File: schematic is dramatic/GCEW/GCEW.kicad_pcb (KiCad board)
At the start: 2 copper layers, 100 x 90 mm, 52 parts, among them J1 Conn_01x08, J2 Conn_01x02, J3 Conn_02x03_Odd_Even, J4 Conn_02x03_Odd_Even, J5 Conn_02x02_Odd_Even, M1 BLDC_Motor, U1 LM26CIM5-VHA, U2 DRV8323RH, U3 IPB029N06N, U4 IPB029N06N, U5 IPB029N06N, U6 IPB029N06N, U7 IPB029N06N, U8 IPB029N06N, U9 BLDC_Hall_Sensor

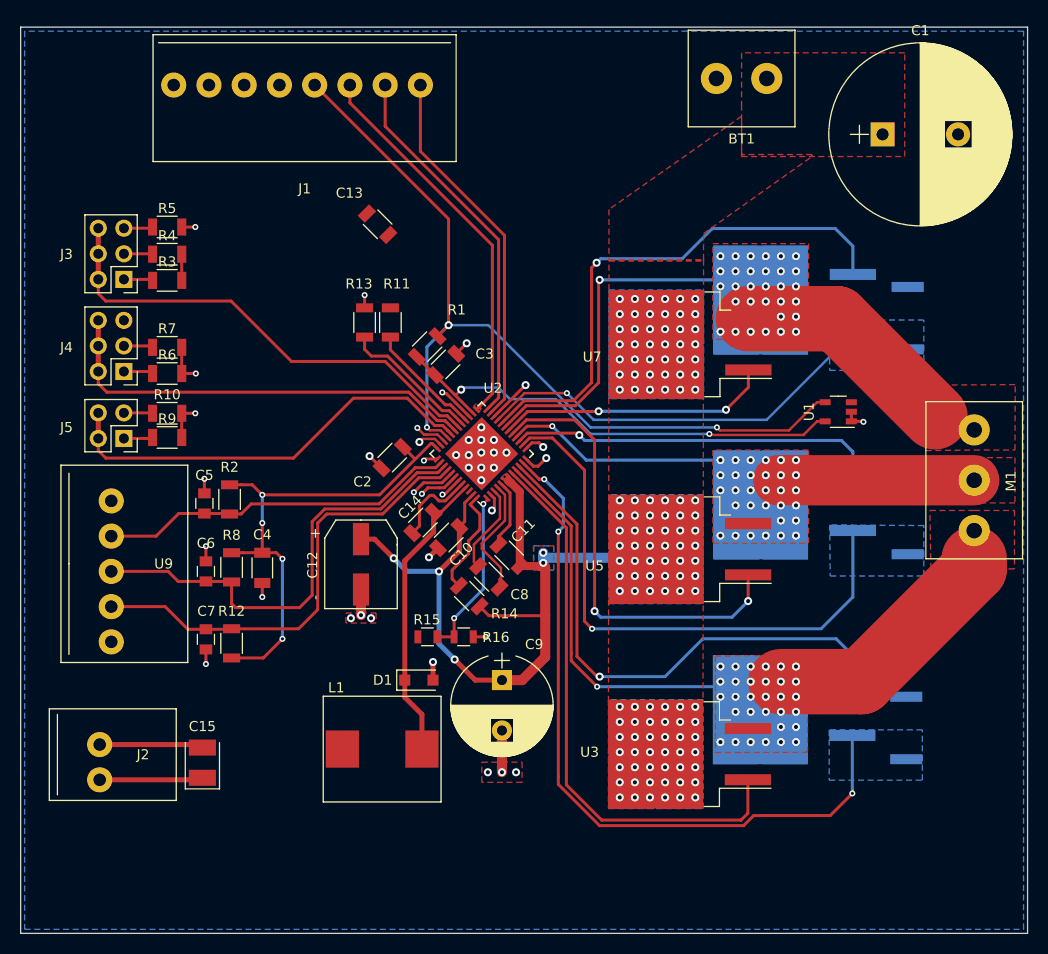
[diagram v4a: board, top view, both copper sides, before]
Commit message: GCEW Motor Controller PCB Update 1
Completed GCEW Motor Controller PCB Design.
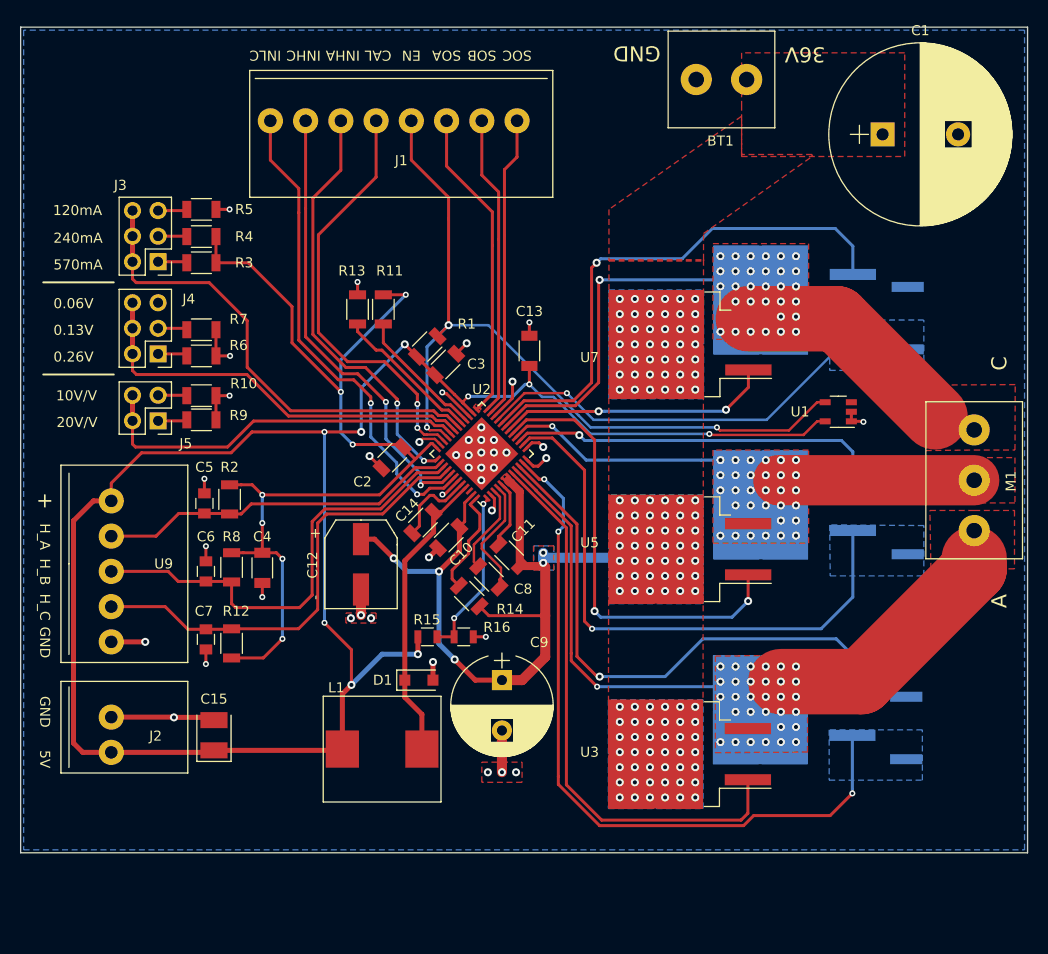
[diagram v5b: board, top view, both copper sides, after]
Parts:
- moved C13 19.6 mm to (165.5, 97.2), turned to 90 degrees
- moved J1 10.2 mm to (152.8, 75.6)
- moved J3 3.82 mm to (128.7, 88.3)
- moved J4 3.82 mm to (128.7, 97.5)
- moved J5 3.82 mm to (128.7, 104.1)
- moved R10 3.82 mm to (132.9, 101.6)
- moved R3 3.82 mm to (132.9, 88.4)
- moved R4 3.82 mm to (132.9, 85.8)
- moved R5 3.82 mm to (132.9, 83.1)
- moved R6 3.82 mm to (132.9, 97.7)
- moved R7 3.82 mm to (132.9, 95.0)
- moved R9 3.82 mm to (132.9, 104.0)
- moved C15 2.96 mm to (134.2, 135.3)
- moved J2 2.96 mm to (125.3, 134.5)
- moved BT1 2.00 mm to (184.6, 70.2)
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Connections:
- J1 pad 6: INLC -> INHA
- J1 pad 8: INHA -> INLC
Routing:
- net VREF: track 57.8 -> 186.5 mm, vias 2 -> 9
- net DVDD: track 52.6 -> 97.7 mm, vias 4 -> 7
- net INLC: track 4.01 -> 47.7 mm, vias 1 -> 2
- net INHA: track 1.41 -> 42.0 mm, vias 1 -> 2
- net INHC: track 4.54 -> 44.5 mm, vias 1 -> 2
- net CAL: track 3.25 -> 42.2 mm, vias 1 -> 2
- net SNA: track 62.3 -> 72.0 mm, vias 40 -> 43
- net SOB: track 37.4 -> 29.7 mm
- net ENABLE: track 87.6 -> 80.1 mm
- net SOA: track 38.7 -> 31.2 mm
- net SOC: track 36.6 -> 30.0 mm
- net GAIN: track 43.1 -> 38.3 mm
- net 36V: track 74.1 -> 77.5 mm
- net VDS: track 43.7 -> 41.3 mm
- net Net-(R11-Pad2): track 11.7 -> 13.2 mm
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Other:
- board size 100 x 90 mm -> 100 x 82 mm
- board text added: "+"
- board text added: "0.06V"
- board text added: "0.13V"
- board text added: "0.26V"
- board text added: "10V/V"
- board text added: "120mA"
- board text added: "20V/V"
- board text added: "240mA"
- board text added: "36V"
- board text added: "570mA"
- board text added: "5V"
- board text added: "A"
- board text added: "C"
- board text added: "CAL"
- board text added: "EN"
- board text added: "GND"
- board text added: "H_A"
- board text added: "H_B"
- board text added: "H_C"
- board text added: "INHA"
- board text added: "INHC"
- board text added: "INLC"
- board text added: "SOA"
- board text added: "SOB"
- board text added: "SOC"
